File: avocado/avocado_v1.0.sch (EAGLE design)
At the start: 99 parts, among them IC1 TM4C129XXXPDT, IC3 MAX31855, IC4 ISO3088, J1 THERMOCOUPLE, U1 LMT87DCKT

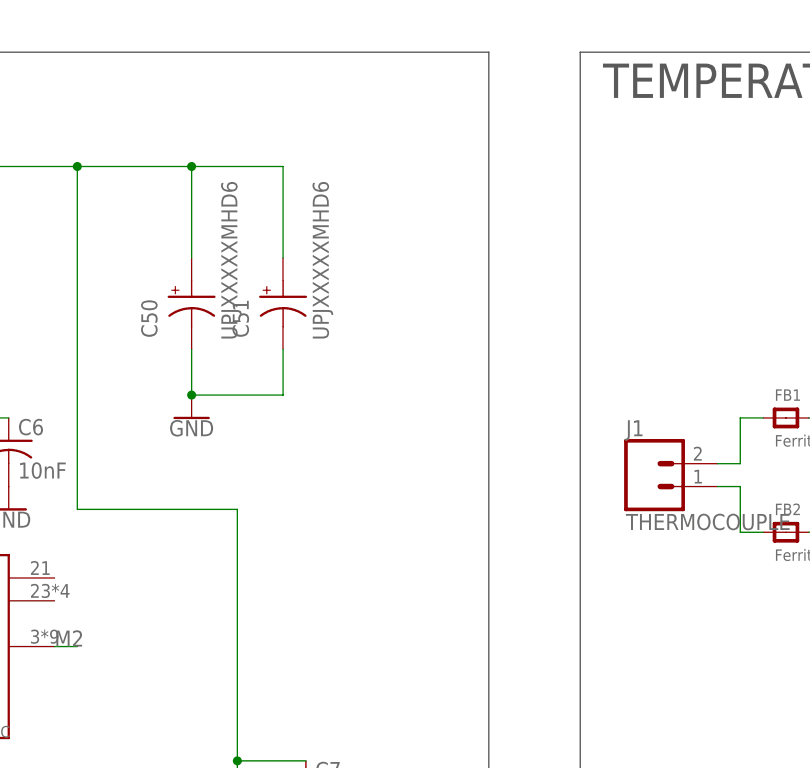
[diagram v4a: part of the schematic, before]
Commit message: removed blind vias and generated new Gerber files
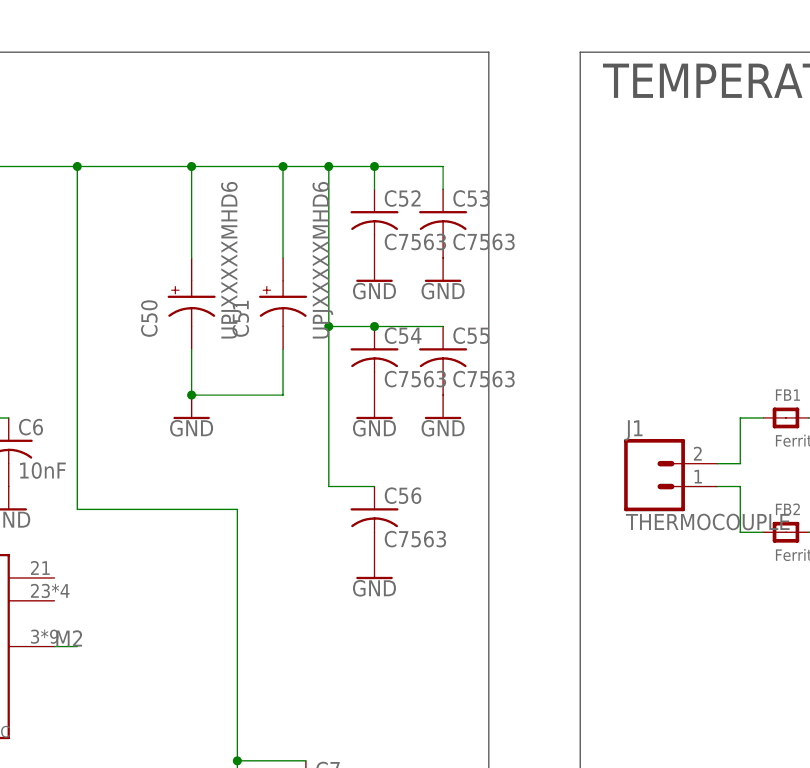
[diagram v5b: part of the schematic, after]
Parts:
- added C52, C53, C54, C55, C56: C7563, avocado:C7563
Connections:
- net 24VDC: now also C52.1, C53.1, C54.1, C55.1, C56.1
- net GND: now also C52.2, C53.2, C54.2, C55.2, C56.2
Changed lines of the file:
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@@
 <part name="R12" library="rcl" library_urn="urn:adsk.eagle:library:334" deviceset="R-US_" device="R0402" package3d_urn="urn:adsk.eagle:package:23547/2" value="10K"/>
 <part name="U$5" library="avocado" deviceset="5040500591" device=""/>
+<part name="C52" library="avocado" deviceset="C7563" device=""/>
+<part name="C53" library="avocado" deviceset="C7563" device=""/>
+<part name="C54" library="avocado" deviceset="C7563" device=""/>
+<part name="C55" library="avocado" deviceset="C7563" device=""/>
+<part name="C56" library="avocado" deviceset="C7563" device=""/>
+<part name="GND11" library="SparkFun-PowerSymbols" deviceset="GND" device=""/>
+<part name="GND35" library="SparkFun-PowerSymbols" deviceset="GND" device=""/>
+<part name="GND36" library="SparkFun-PowerSymbols" deviceset="GND" device=""/>
+<part name="GND37" library="SparkFun-PowerSymbols" deviceset="GND" device=""/>
+<part name="GND38" library="SparkFun-PowerSymbols" deviceset="GND" device=""/>
 </parts>
 <sheets>
@@
 </instance>
 <instance part="U$5" gate="G$1" x="-167.64" y="-10.16"/>
+<instance part="C52" gate="G$1" x="111.76" y="-71.12"/>
+<instance part="C53" gate="G$1" x="119.38" y="-71.12"/>
+<instance part="C54" gate="G$1" x="111.76" y="-86.36"/>
+<instance part="C55" gate="G$1" x="119.38" y="-86.36"/>
+<instance part="C56" gate="G$1" x="111.76" y="-104.14"/>
+<instance part="GND11" gate="1" x="111.76" y="-78.74"/>
+<instance part="GND35" gate="1" x="119.38" y="-78.74"/>
+<instance part="GND36" gate="1" x="111.76" y="-93.98"/>
+<instance part="GND37" gate="1" x="119.38" y="-93.98"/>
+<instance part="GND38" gate="1" x="111.76" y="-111.76"/>
 </instances>
 <busses>
@@
 <pinref part="C51" gate="G$1" pin="A"/>
 <wire x1="101.6" y1="-66.04" x2="101.6" y2="-76.2" width="0.1524" layer="91"/>
+<pinref part="C52" gate="G$1" pin="1"/>
+<wire x1="101.6" y1="-66.04" x2="106.68" y2="-66.04" width="0.1524" layer="91"/>
+<wire x1="106.68" y1="-66.04" x2="111.76" y2="-66.04" width="0.1524" layer="91"/>
+<wire x1="111.76" y1="-66.04" x2="111.76" y2="-68.58" width="0.1524" layer="91"/>
+<junction x="101.6" y="-66.04"/>
+<pinref part="C53" gate="G$1" pin="1"/>
+<wire x1="111.76" y1="-66.04" x2="119.38" y2="-66.04" width="0.1524" layer="91"/>
+<wire x1="119.38" y1="-66.04" x2="119.38" y2="-68.58" width="0.1524" layer="91"/>
+<junction x="111.76" y="-66.04"/>
+<wire x1="106.68" y1="-66.04" x2="106.68" y2="-83.82" width="0.1524" layer="91"/>
+<junction x="106.68" y="-66.04"/>
+<pinref part="C54" gate="G$1" pin="1"/>
+<wire x1="106.68" y1="-83.82" x2="111.76" y2="-83.82" width="0.1524" layer="91"/>
+<pinref part="C55" gate="G$1" pin="1"/>
+<wire x1="111.76" y1="-83.82" x2="119.38" y2="-83.82" width="0.1524" layer="91"/>
+<junction x="111.76" y="-83.82"/>
+<wire x1="106.68" y1="-83.82" x2="106.68" y2="-101.6" width="0.1524" layer="91"/>
+<junction x="106.68" y="-83.82"/>
+<pinref part="C56" gate="G$1" pin="1"/>
+<wire x1="106.68" y1="-101.6" x2="111.76" y2="-101.6" width="0.1524" layer="91"/>
 </segment>
 <segment>
@@
 <label x="-160.02" y="-12.7" size="1.778" layer="95"/>
 </segment>
+<segment>
+<pinref part="C52" gate="G$1" pin="2"/>
+<pinref part="GND11" gate="1" pin="GND"/>
+</segment>
+<segment>
+<pinref part="C53" gate="G$1" pin="2"/>
+<pinref part="GND35" gate="1" pin="GND"/>
+</segment>
+<segment>
+<pinref part="C54" gate="G$1" pin="2"/>
+<pinref part="GND36" gate="1" pin="GND"/>
+</segment>
+<segment>
+<pinref part="C55" gate="G$1" pin="2"/>
+<pinref part="GND37" gate="1" pin="GND"/>
+</segment>
+<segment>
+<pinref part="C56" gate="G$1" pin="2"/>
+<pinref part="GND38" gate="1" pin="GND"/>
+</segment>
 </net>
